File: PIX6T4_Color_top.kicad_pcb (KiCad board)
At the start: 2 copper layers, 88.9 x 33 mm, 78 parts

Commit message: Rev. 2
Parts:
- added G***: LOGO, LOGO, F.Cu at (161.0, 106.6)
- REF** (x10): value MountingHole_6mm -> MountingHole_6mm_tight; footprint MountingHole:MountingHole_6mm -> Library:MountingHole_6mm_tight
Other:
- outline, holes or cut-outs redrawn
- board text added: "Color"
- board text added: "PIX6T4"

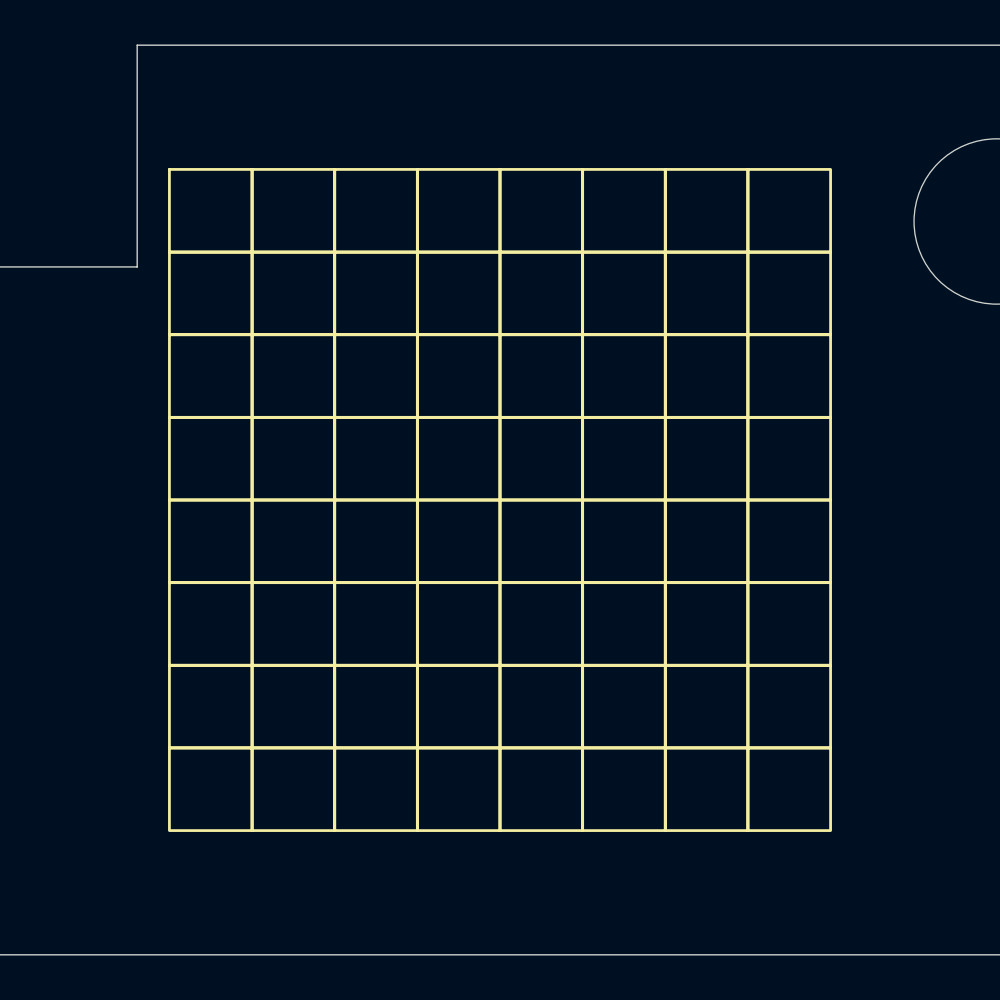
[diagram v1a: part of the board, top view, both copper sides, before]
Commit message: Add power / invader logo light
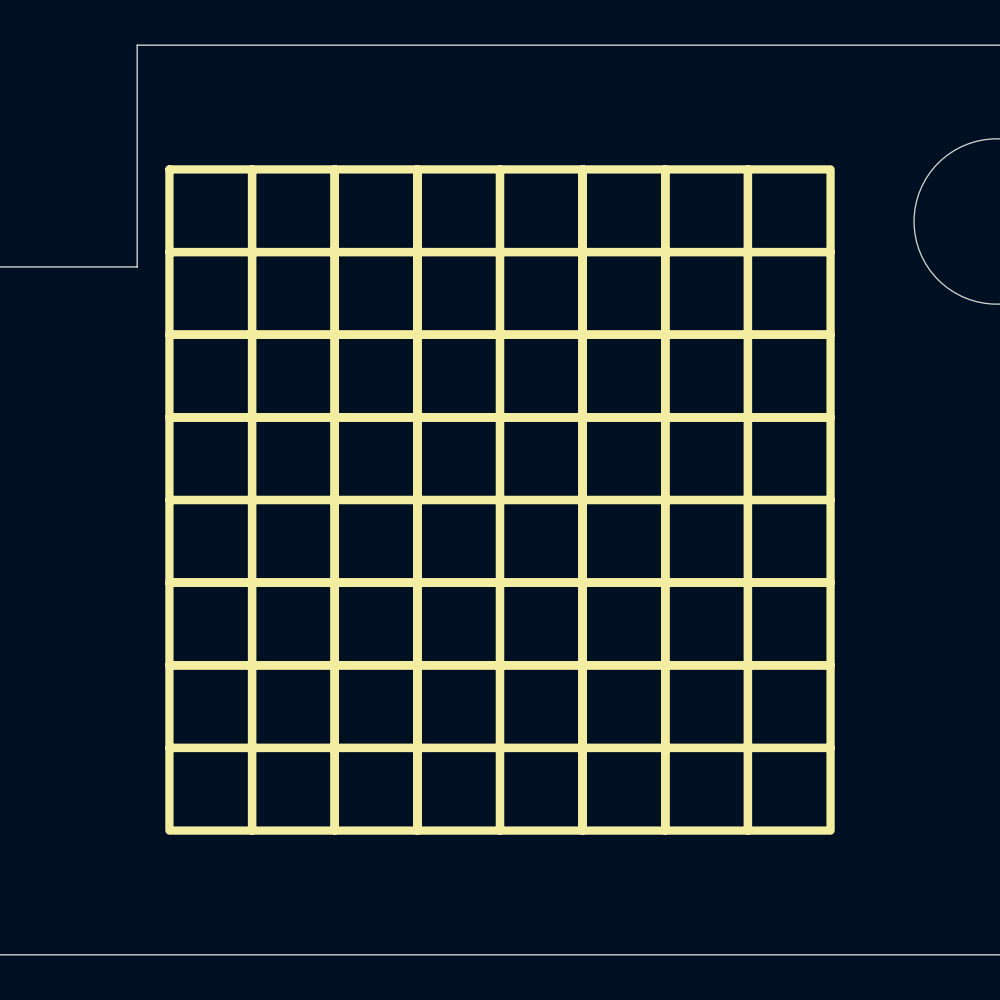
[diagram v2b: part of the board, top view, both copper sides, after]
